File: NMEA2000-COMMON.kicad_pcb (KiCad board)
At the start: 2 copper layers, 100 x 85 mm, 72 parts, among them J2 CAN, SW1 PRG, SW2 INSTANCE, SW3 BUS, U1 MCP2551-I-P, U101 74LS165, U2 TMR-2-2411, U3 74HCT595, U4 74HCT595, U5 Teensy_4.0

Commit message: Tweak
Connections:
- net /TRANSMIT_LED renamed Net-(D5-Pad2)

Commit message: Reroute
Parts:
- U101: value 74LS165 -> 74HC165
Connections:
- U101 pad 10: Net-(U101-Pad10) -> GND
- U101 pad 15: /INSTANCE_CE -> GND
- U5 pad 11: /INSTANCE_CE -> /D9
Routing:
- net GND: track 7.75 -> 50.0 mm, vias 38 -> 29
- net /D9: track 0.00 -> 33.5 mm, vias 0 -> 1
- net /INSTANCE_CE: track 17.1 -> 0.00 mm, vias 1 -> 0
- net /CAN_RX: track 45.9 -> 56.8 mm
- net /CAN_TX: track 53.7 -> 63.4 mm
- net /D23: track 10.5 -> 14.6 mm
- net /D22: track 14.1 -> 18.1 mm
- net /D6: track 21.7 -> 25.6 mm
- net /D5: track 18.1 -> 21.5 mm
- net /D8: track 28.9 -> 30.1 mm
- net /D7: track 25.3 -> 26.4 mm
- net /D21: track 17.8 -> 18.8 mm
- net /D19: track 24.9 -> 25.9 mm
- net /D18: track 28.4 -> 29.5 mm
- net /D16: track 35.5 -> 36.5 mm
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
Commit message: Reroute PISO
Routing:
- net GND: track 50.0 -> 63.4 mm, vias 29 -> 28
- net Net-(R107-Pad2): track 15.1 -> 11.8 mm
- net Net-(R108-Pad2): track 15.2 -> 13.1 mm
- net Net-(R105-Pad2): track 15.2 -> 16.9 mm
- net /INSTANCE_PL: track 27.0 -> 28.3 mm, vias 1 -> 3
- net Net-(R103-Pad2): track 14.2 -> 15.1 mm
- net /INSTANCE_CP: track 28.8 -> 29.5 mm, vias 1 -> 3
- net Net-(R102-Pad2): track 15.8 -> 16.4 mm
- net Net-(R106-Pad2): track 14.8 -> 14.3 mm
- net Net-(R101-Pad2): track 17.2 -> 17.3 mm, vias 0 -> 1
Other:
- board text added: "D23 - D16"
- board text added: "D9 - D5"

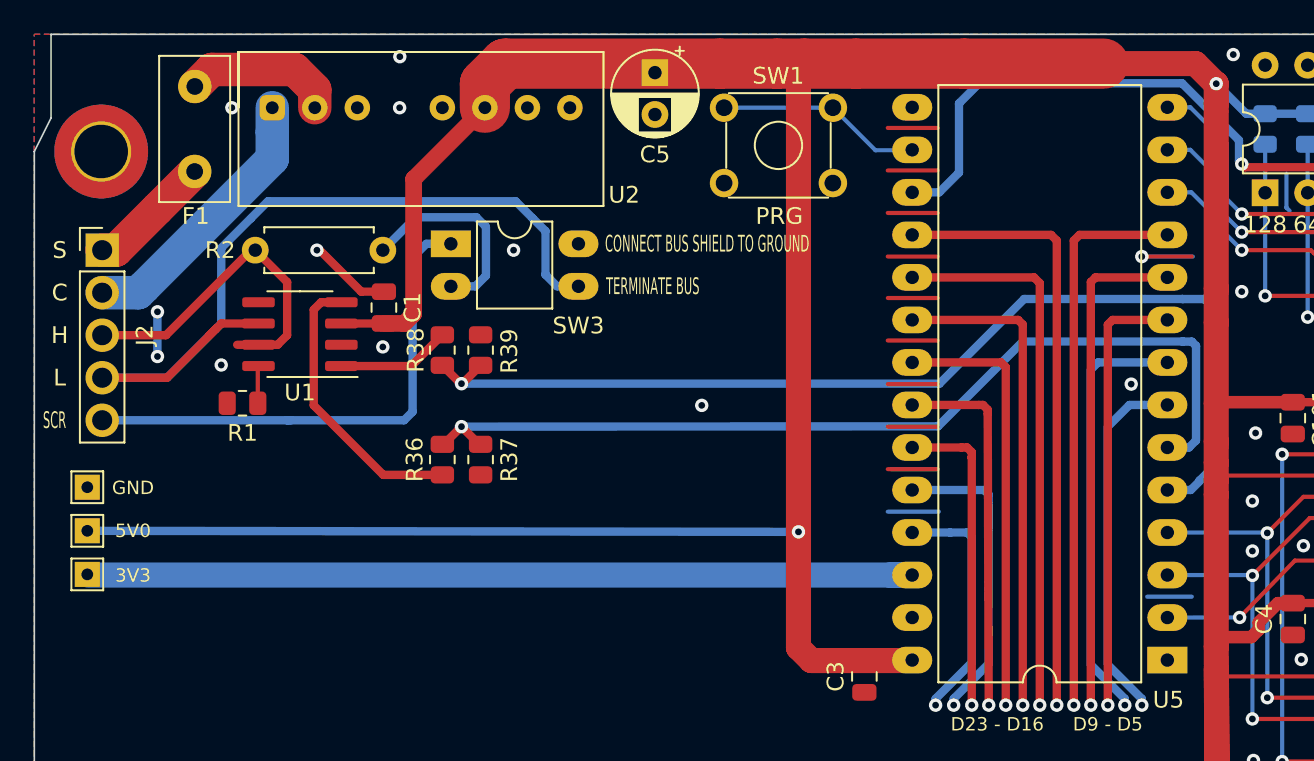
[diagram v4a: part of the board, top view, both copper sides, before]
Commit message: Add level shifters
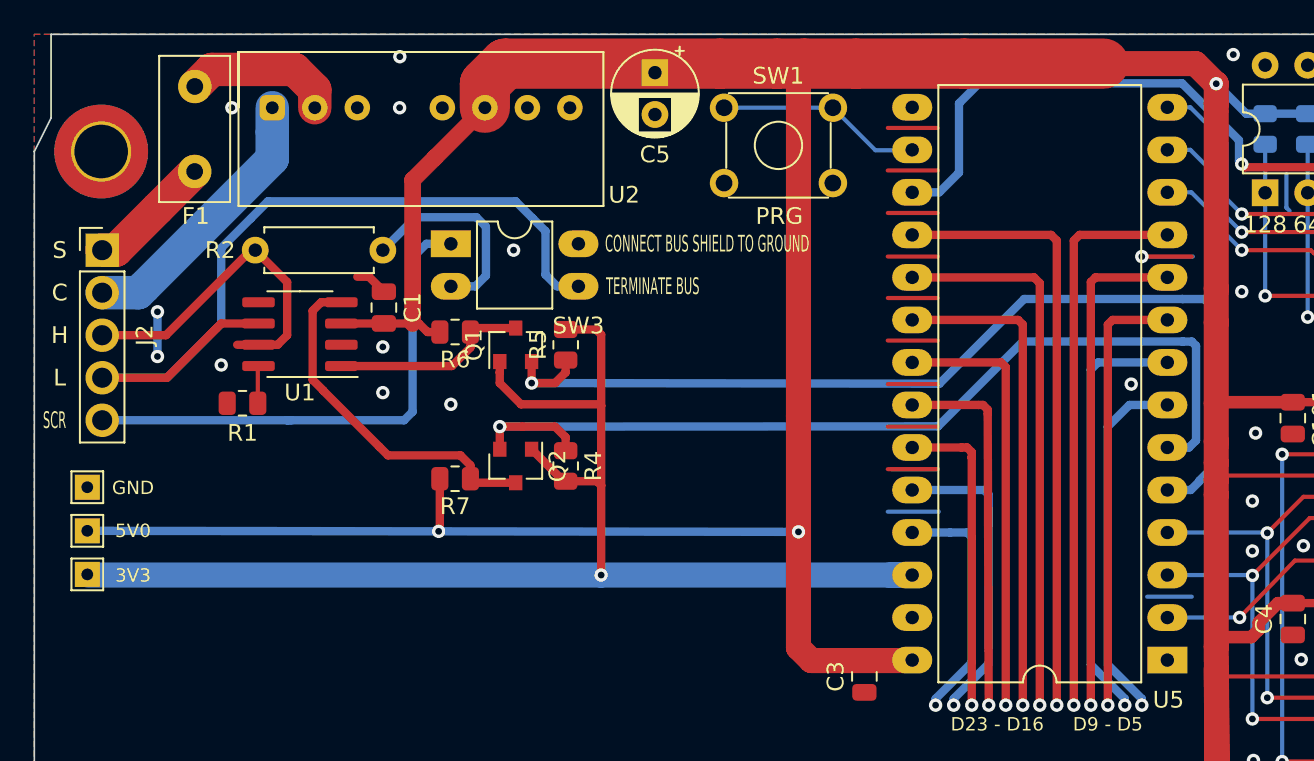
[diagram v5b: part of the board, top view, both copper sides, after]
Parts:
- removed R36, R38: 2K2 0.125W, Resistor_SMD:R_0805_2012Metric
- removed R37, R39: 3K3 0.125W, Resistor_SMD:R_0805_2012Metric
- added Q1: BSS138, Package_TO_SOT_SMD:SOT-23, F.Cu at (48.8, 38.5)
- added Q2: BSS138, Package_TO_SOT_SMD:SOT-23, F.Cu at (48.8, 45.8)
- added R4: 4K7 0.125W, Resistor_SMD:R_0805_2012Metric, F.Cu at (51.7, 45.8)
- added R5: 4K7 0.125W, Resistor_SMD:R_0805_2012Metric, F.Cu at (51.7, 38.5)
- added R6: 4K7 0.125W, Resistor_SMD:R_0805_2012Metric, F.Cu at (45.1, 37.8)
- added R7: 4K7 0.125W, Resistor_SMD:R_0805_2012Metric, F.Cu at (45.1, 46.5)
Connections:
- U1 pad 1: /CAN_TX_3V3 -> Net-(Q1-Pad3)
- U1 pad 4: /CAN_RX_3V3 -> Net-(Q2-Pad3)
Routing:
- net +3V3: track 50.6 -> 80.2 mm, vias 0 -> 1
- net Net-(Q2-Pad3): track 0.00 -> 21.2 mm
- net /CAN_RX_3V3: track 17.0 -> 0.00 mm
- net Net-(Q1-Pad3): track 0.00 -> 11.9 mm
- net /CAN_TX_3V3: track 6.81 -> 0.00 mm
- net +5V: track 264.2 -> 269.5 mm, vias 2 -> 3
- net /CAN_TX: track 63.4 -> 60.1 mm
- net GND: track 63.4 -> 60.3 mm
- net /CAN_RX: track 56.8 -> 57.7 mm

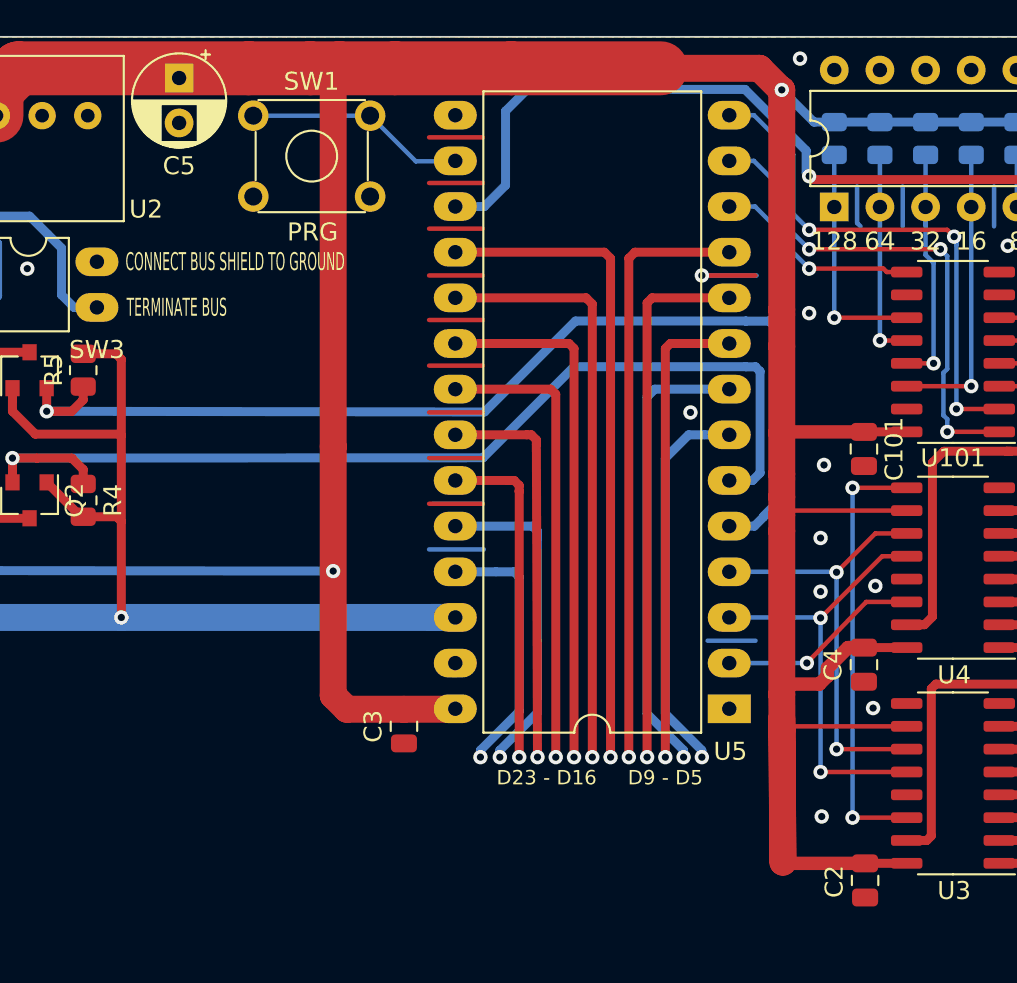
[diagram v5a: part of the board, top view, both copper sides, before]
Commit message: Revise logic shifter R values
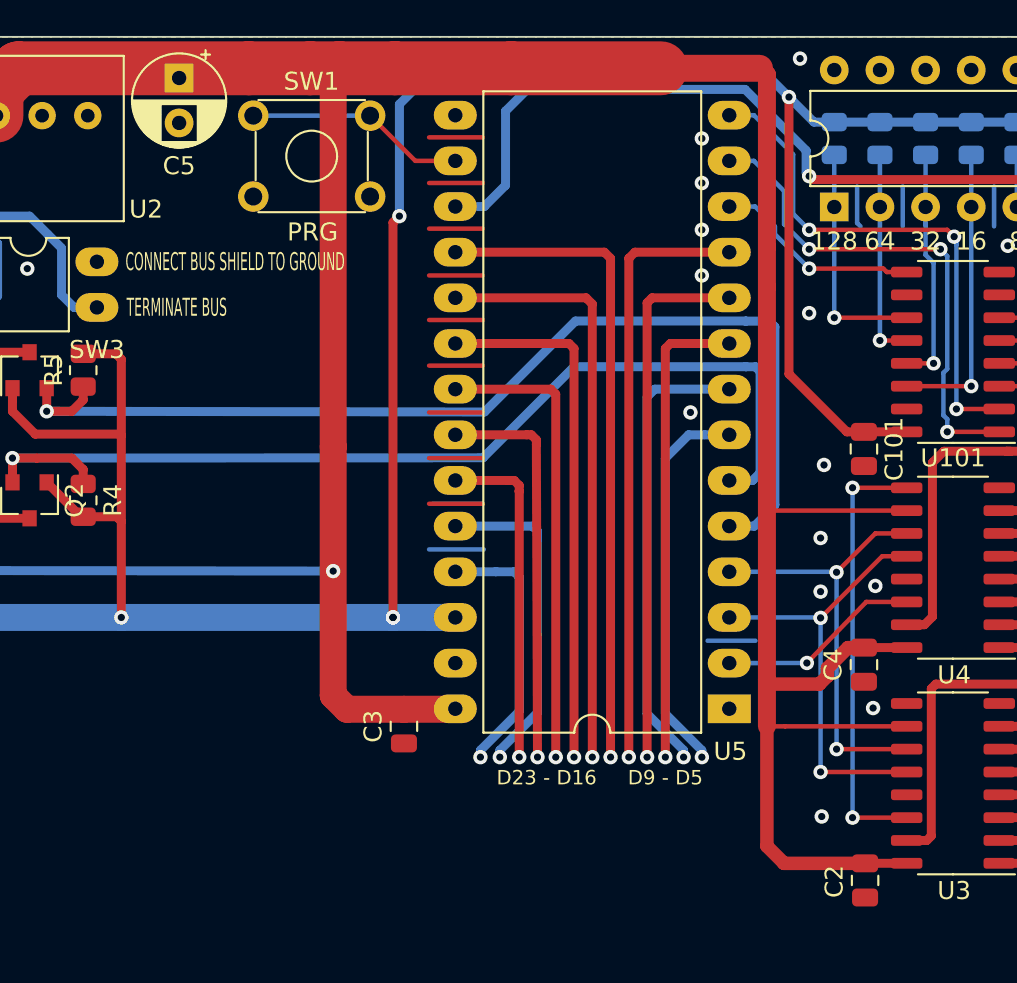
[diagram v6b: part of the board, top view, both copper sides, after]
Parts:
- R4, R5, R6, R7: value 4K7 0.125W -> 10K 0.125W
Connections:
- C101 pad 1: +5V -> +3V3
- R101 pad 1: +5V -> +3V3
- R102 pad 1: +5V -> +3V3
- R103 pad 1: +5V -> +3V3
- R104 pad 1: +5V -> +3V3
- R105 pad 1: +5V -> +3V3
- R106 pad 1: +5V -> +3V3
- R107 pad 1: +5V -> +3V3
- R108 pad 1: +5V -> +3V3
- U101 pad 16: +5V -> +3V3
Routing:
- net +3V3: track 80.2 -> 176.2 mm, vias 1 -> 5
- net +5V: track 269.5 -> 233.2 mm, vias 3 -> 2
- net GND: track 60.3 -> 54.3 mm, vias 28 -> 31

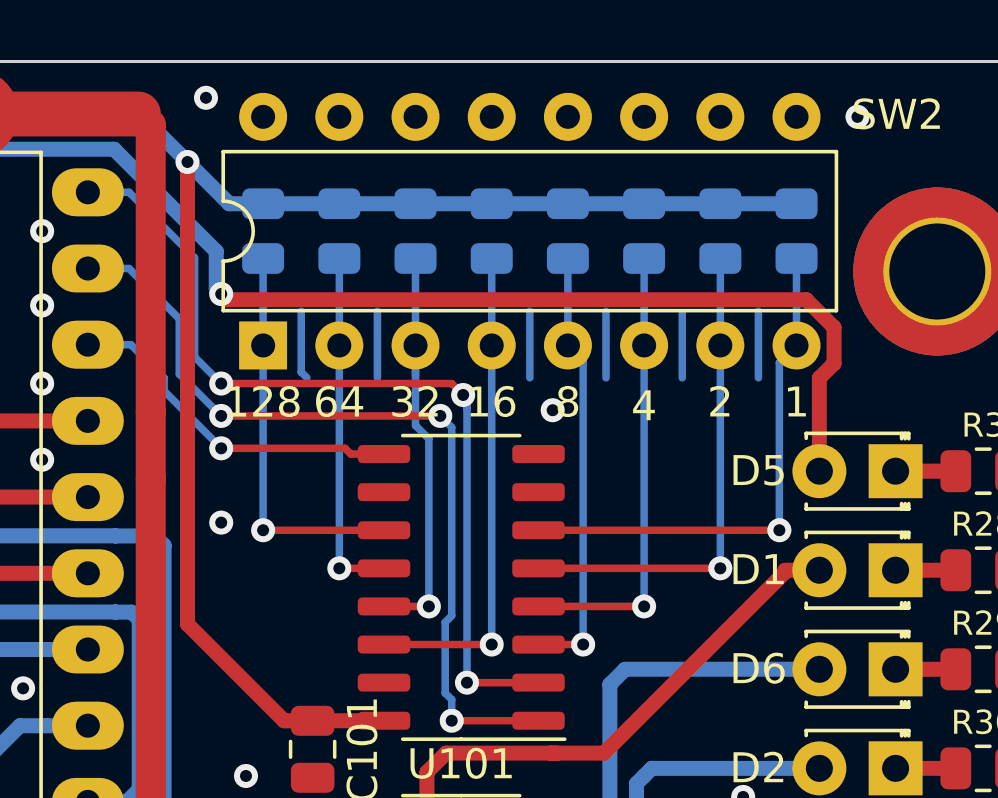
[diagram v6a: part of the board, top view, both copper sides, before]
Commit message: Move PISO to 3.3VDC
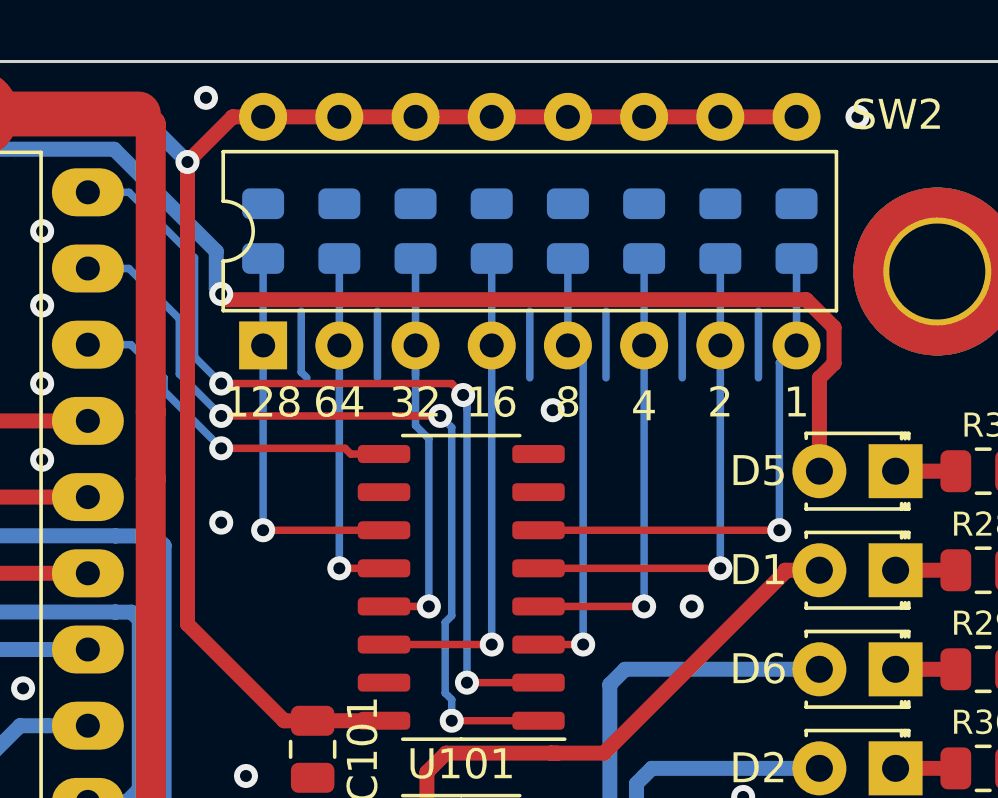
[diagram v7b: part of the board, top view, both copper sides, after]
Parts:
- turned R101 to 90 degrees
- turned R102 to 90 degrees
- turned R103 to 90 degrees
- turned R104 to 90 degrees
- turned R105 to 90 degrees
- turned R106 to 90 degrees
- turned R107 to 90 degrees
- turned R108 to 90 degrees
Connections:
- R101 pad 1: +3V3 -> Net-(R101-Pad1)
- R101 pad 2: Net-(R101-Pad2) -> GND
- R102 pad 1: +3V3 -> Net-(R102-Pad1)
- R102 pad 2: Net-(R102-Pad2) -> GND
- R103 pad 1: +3V3 -> Net-(R103-Pad1)
- R103 pad 2: Net-(R103-Pad2) -> GND
- R104 pad 1: +3V3 -> Net-(R104-Pad1)
- R104 pad 2: Net-(R104-Pad2) -> GND
- R105 pad 1: +3V3 -> Net-(R105-Pad1)
- R105 pad 2: Net-(R105-Pad2) -> GND
- R106 pad 1: +3V3 -> Net-(R106-Pad1)
- R106 pad 2: Net-(R106-Pad2) -> GND
- R107 pad 1: +3V3 -> Net-(R107-Pad1)
- R107 pad 2: Net-(R107-Pad2) -> GND
- R108 pad 1: +3V3 -> Net-(R108-Pad1)
- R108 pad 2: Net-(R108-Pad2) -> GND
- SW2 pad 1: Net-(R108-Pad2) -> Net-(R108-Pad1)
- SW2 pad 10: GND -> +3V3
- SW2 pad 11: GND -> +3V3
- SW2 pad 12: GND -> +3V3
- SW2 pad 13: GND -> +3V3
- SW2 pad 14: GND -> +3V3
- SW2 pad 15: GND -> +3V3
- SW2 pad 16: GND -> +3V3
- SW2 pad 2: Net-(R107-Pad2) -> Net-(R107-Pad1)
- SW2 pad 3: Net-(R106-Pad2) -> Net-(R106-Pad1)
- SW2 pad 4: Net-(R105-Pad2) -> Net-(R105-Pad1)
- SW2 pad 5: Net-(R104-Pad2) -> Net-(R104-Pad1)
- SW2 pad 6: Net-(R103-Pad2) -> Net-(R103-Pad1)
- SW2 pad 7: Net-(R102-Pad2) -> Net-(R102-Pad1)
- SW2 pad 8: Net-(R101-Pad2) -> Net-(R101-Pad1)
- SW2 pad 9: GND -> +3V3
- U101 pad 11: Net-(R108-Pad2) -> Net-(R108-Pad1)
- U101 pad 12: Net-(R107-Pad2) -> Net-(R107-Pad1)
- U101 pad 13: Net-(R106-Pad2) -> Net-(R106-Pad1)
- U101 pad 14: Net-(R105-Pad2) -> Net-(R105-Pad1)
- U101 pad 3: Net-(R104-Pad2) -> Net-(R104-Pad1)
- U101 pad 4: Net-(R103-Pad2) -> Net-(R103-Pad1)
- U101 pad 5: Net-(R102-Pad2) -> Net-(R102-Pad1)
- U101 pad 6: Net-(R101-Pad2) -> Net-(R101-Pad1)
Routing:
- net Net-(R101-Pad2): track 17.3 -> 0.00 mm, vias 1 -> 0
- net Net-(R101-Pad1): track 0.00 -> 17.3 mm, vias 0 -> 1
- net Net-(R105-Pad2): track 16.9 -> 0.00 mm, vias 1 -> 0
- net Net-(R105-Pad1): track 0.00 -> 16.9 mm, vias 0 -> 1
- net Net-(R102-Pad2): track 16.4 -> 0.00 mm, vias 1 -> 0
- net Net-(R102-Pad1): track 0.00 -> 16.4 mm, vias 0 -> 1
- net Net-(R103-Pad2): track 15.1 -> 0.00 mm, vias 1 -> 0
- net Net-(R103-Pad1): track 0.00 -> 15.1 mm, vias 0 -> 1
- net Net-(R104-Pad2): track 15.1 -> 0.00 mm, vias 1 -> 0
- net Net-(R104-Pad1): track 0.00 -> 15.1 mm, vias 0 -> 1
- net Net-(R106-Pad2): track 14.3 -> 0.00 mm, vias 1 -> 0
- net Net-(R106-Pad1): track 0.00 -> 14.3 mm, vias 0 -> 1
- net Net-(R108-Pad2): track 13.1 -> 0.00 mm, vias 1 -> 0
- net Net-(R108-Pad1): track 0.00 -> 13.1 mm, vias 0 -> 1
- net Net-(R107-Pad2): track 11.8 -> 0.00 mm, vias 1 -> 0
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
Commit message: Schematic tidy up
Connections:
- net /LED_SER renamed Net-(U3-Pad14)
- C1 pad 2: GND -> +5V
- C101 pad 2: GND -> +5V
- C2 pad 2: GND -> +5V
- C3 pad 2: GND -> +5V
- C4 pad 2: GND -> +5V
- C5 pad 2: GND -> +5V
- R1 pad 1: GND -> +5V
- R101 pad 2: GND -> +5V
- R102 pad 2: GND -> +5V
- R103 pad 2: GND -> +5V
- R104 pad 2: GND -> +5V
- R105 pad 2: GND -> +5V
- R106 pad 2: GND -> +5V
- R107 pad 2: GND -> +5V
- R108 pad 2: GND -> +5V
- R28 pad 2: GND -> +5V
- R29 pad 2: GND -> +5V
- R3 pad 2: GND -> +5V
- R30 pad 2: GND -> +5V
- R31 pad 2: GND -> +5V
- R32 pad 2: GND -> +5V
- R33 pad 2: GND -> +5V
- R34 pad 2: GND -> +5V
- R35 pad 2: GND -> +5V
- R40 pad 2: GND -> +5V
- R41 pad 2: GND -> +5V
- R42 pad 2: GND -> +5V
- R43 pad 2: GND -> +5V
- R44 pad 2: GND -> +5V
- R45 pad 2: GND -> +5V
- R46 pad 2: GND -> +5V
- R47 pad 2: GND -> +5V
- SW1 pad 3: GND -> +5V
- SW1 pad 4: GND -> +5V
- SW3 pad 4: GND -> +5V
- U1 pad 2: GND -> +5V
- U101 pad 10: GND -> +5V
- U101 pad 15: GND -> +5V
- U101 pad 8: GND -> +5V
- U2 pad 7: GND -> +5V
- U3 pad 13: GND -> +5V
- U3 pad 8: GND -> +5V
- U4 pad 13: GND -> +5V
- U4 pad 8: GND -> +5V
- U5 pad 1: GND -> +5V
- U5 pad 27: GND -> +5V
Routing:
- net GND: track 54.3 -> 0.00 mm, vias 32 -> 0
- net +5V: track 233.2 -> 287.4 mm, vias 2 -> 34
- added copper zone on B.Cu, net +5V
- added copper zone on F.Cu, net +5V
- removed copper zone on B.Cu, net GND
- removed copper zone on F.Cu, net GND
